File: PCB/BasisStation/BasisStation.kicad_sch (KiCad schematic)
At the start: 2 parts, among them U1 ESP32-S3-WROOM-1

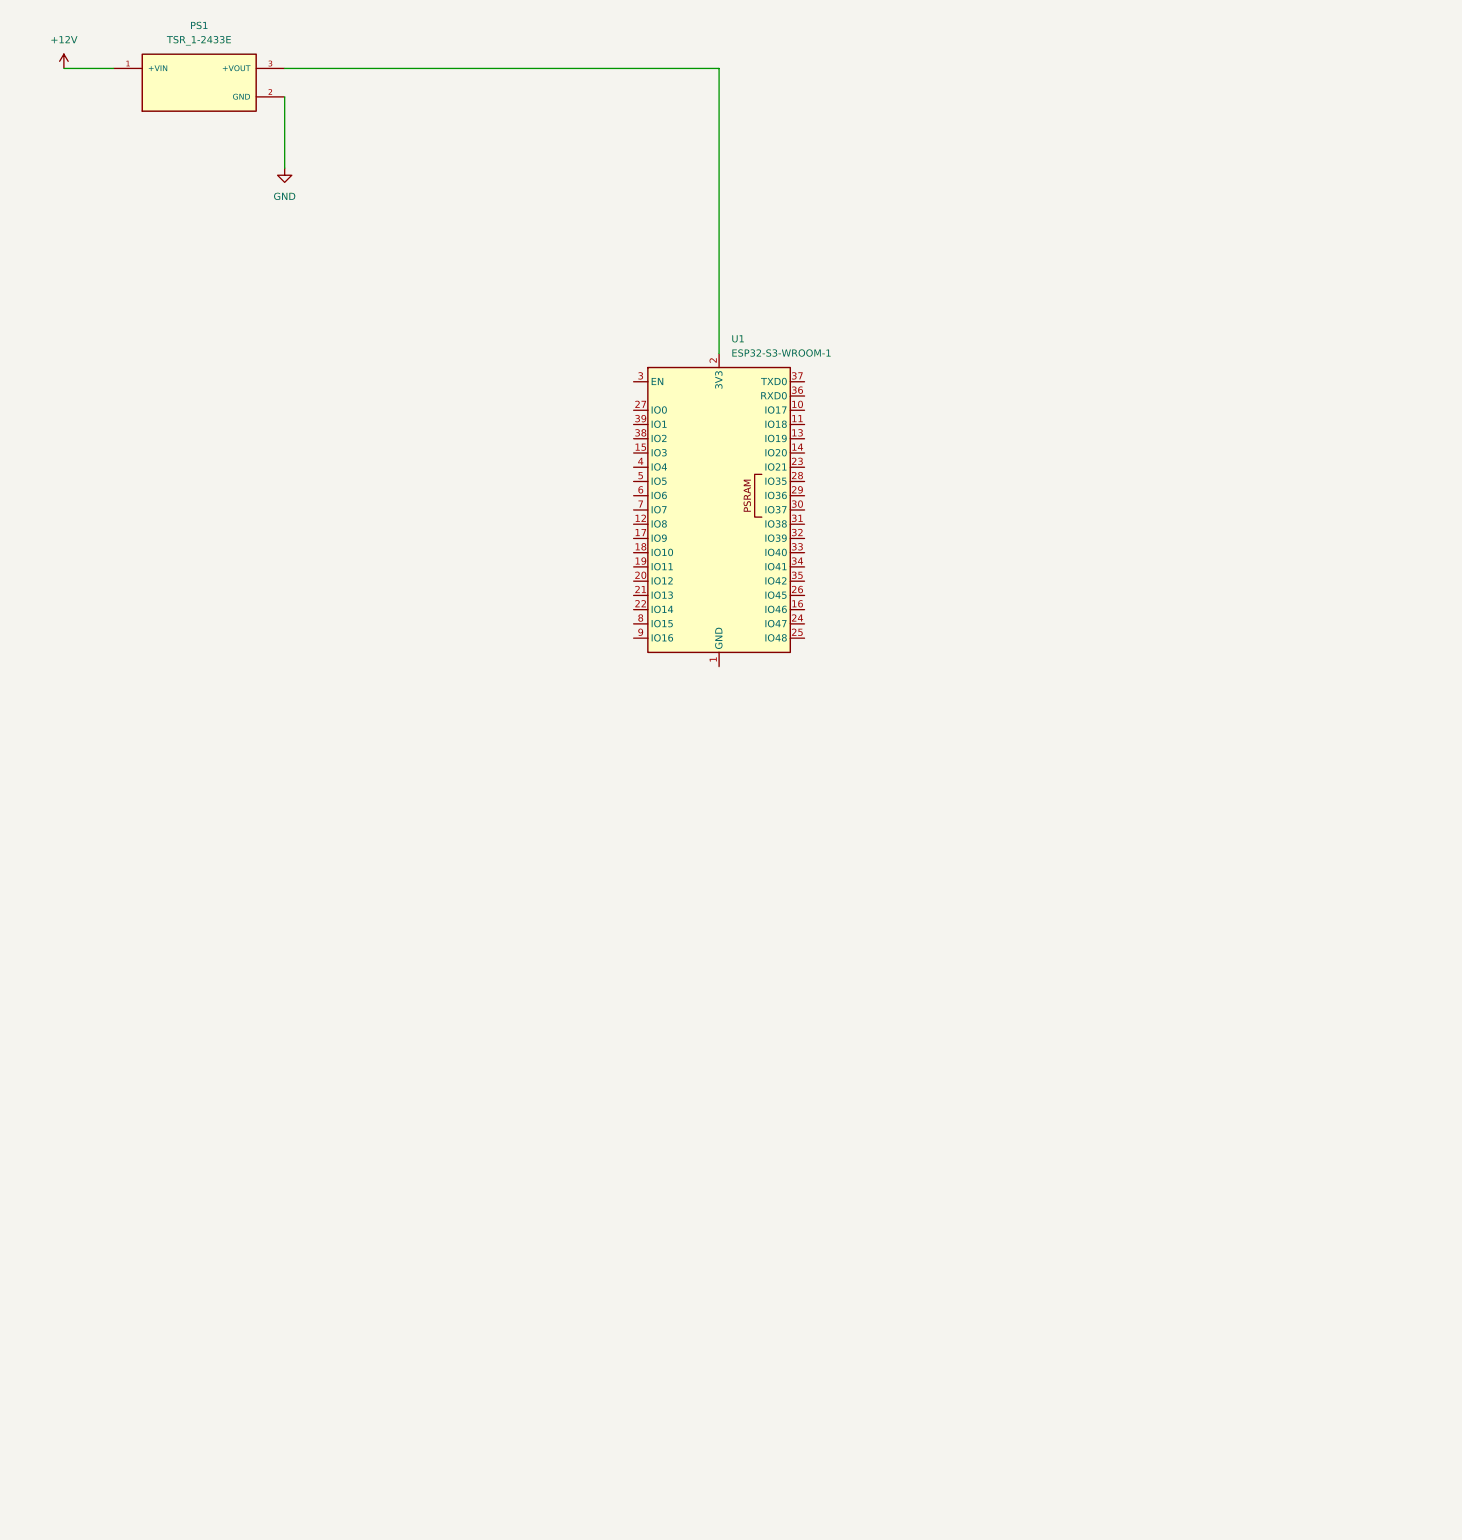
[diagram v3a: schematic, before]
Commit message: ESP32 Microcontroller geändert
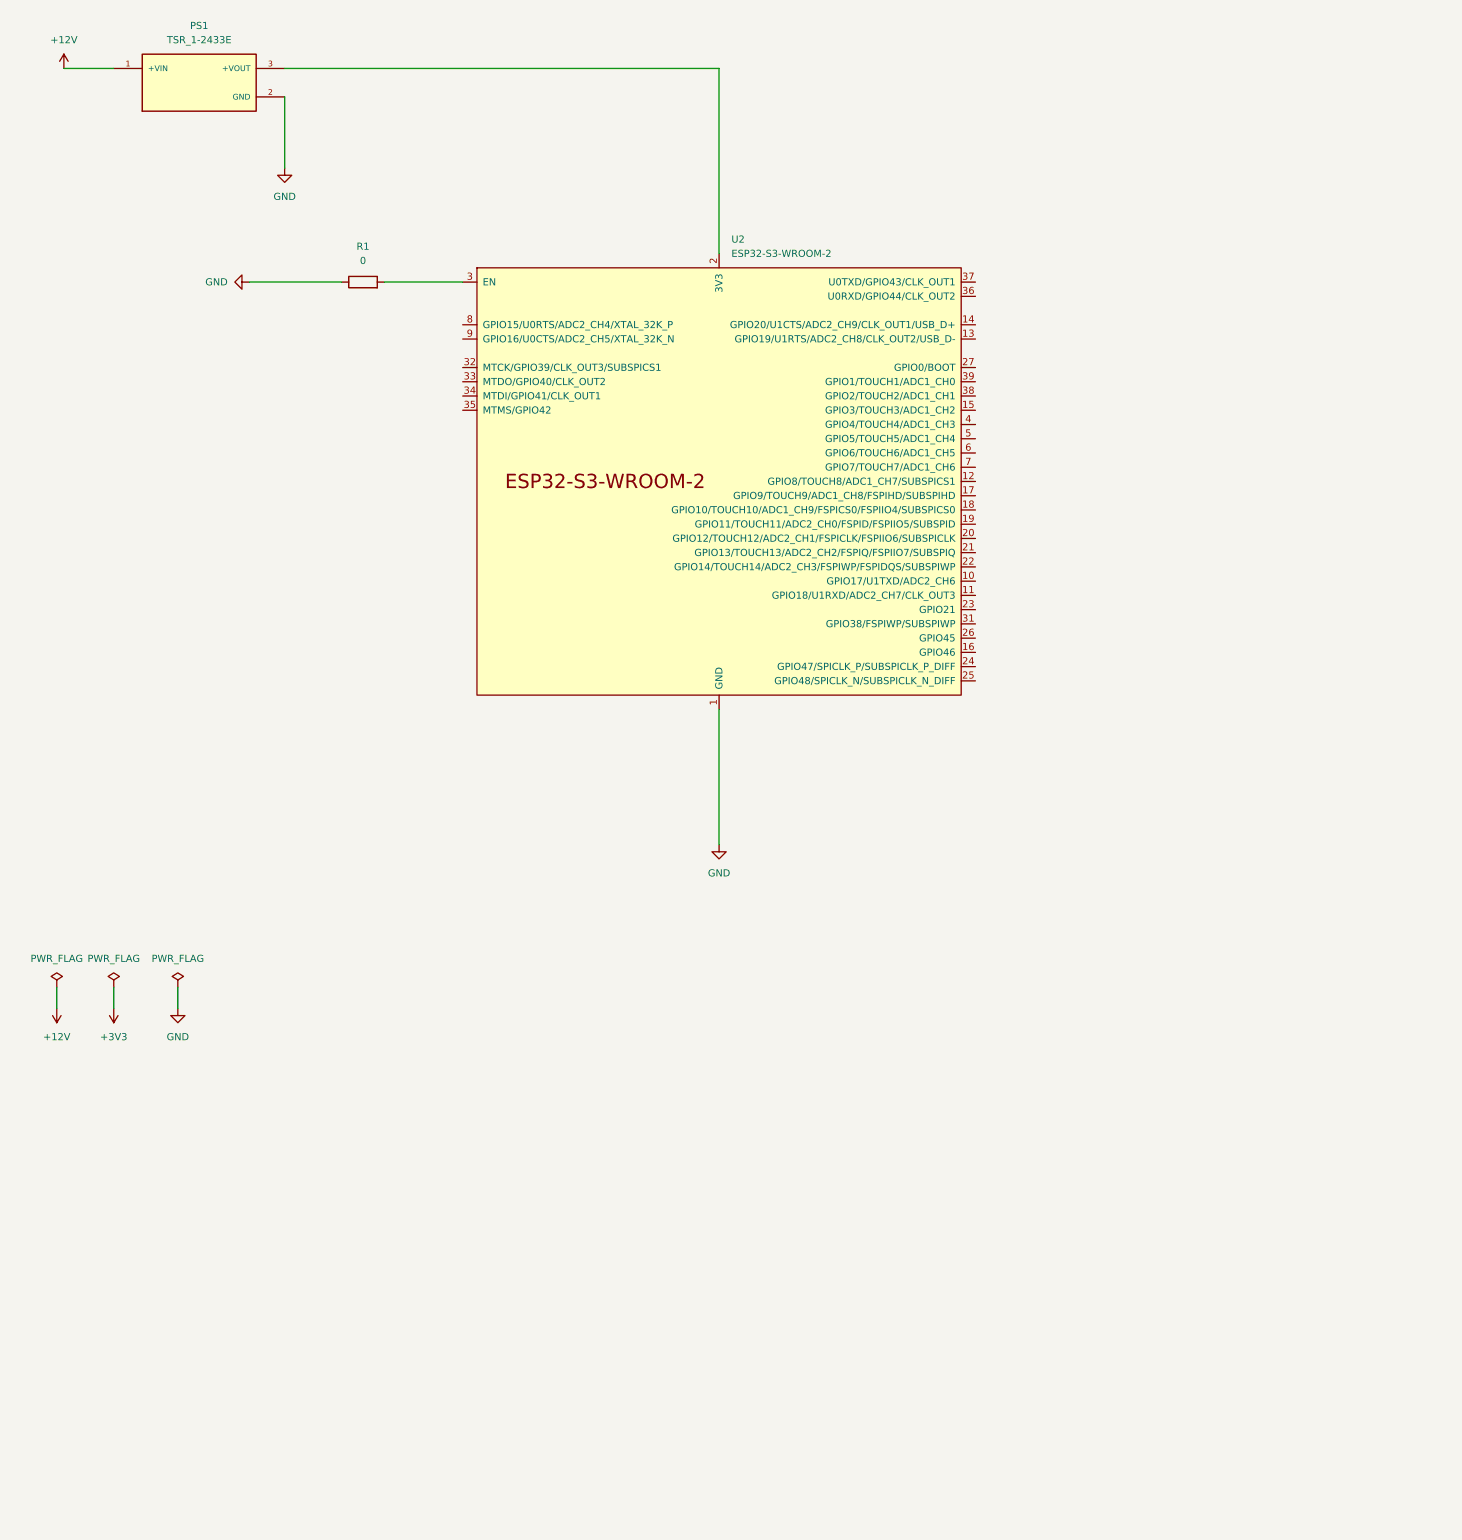
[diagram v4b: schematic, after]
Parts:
- removed U1: ESP32-S3-WROOM-1, RF_Module:ESP32-S3-WROOM-1, symbol RF_Module:ESP32-S3-WROOM-1
- added R1: 0, Resistor_THT:R_Axial_DIN0207_L6.3mm_D2.5mm_P10.16mm_Horizontal, symbol Device:R
- added U2: ESP32-S3-WROOM-2, PCM_Espressif:ESP32-S3-WROOM-2, symbol PCM_Espressif:ESP32-S3-WROOM-2
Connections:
- net GND: now also R1.1, U2.1 (GND), U2.40 (GND), U2.41 (GND)
- net at PS1.3 (+VOUT): now also U2.2 (3V3)
- new net: R1.2, U2.3 (EN)

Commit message: schaltplan überarbeitete
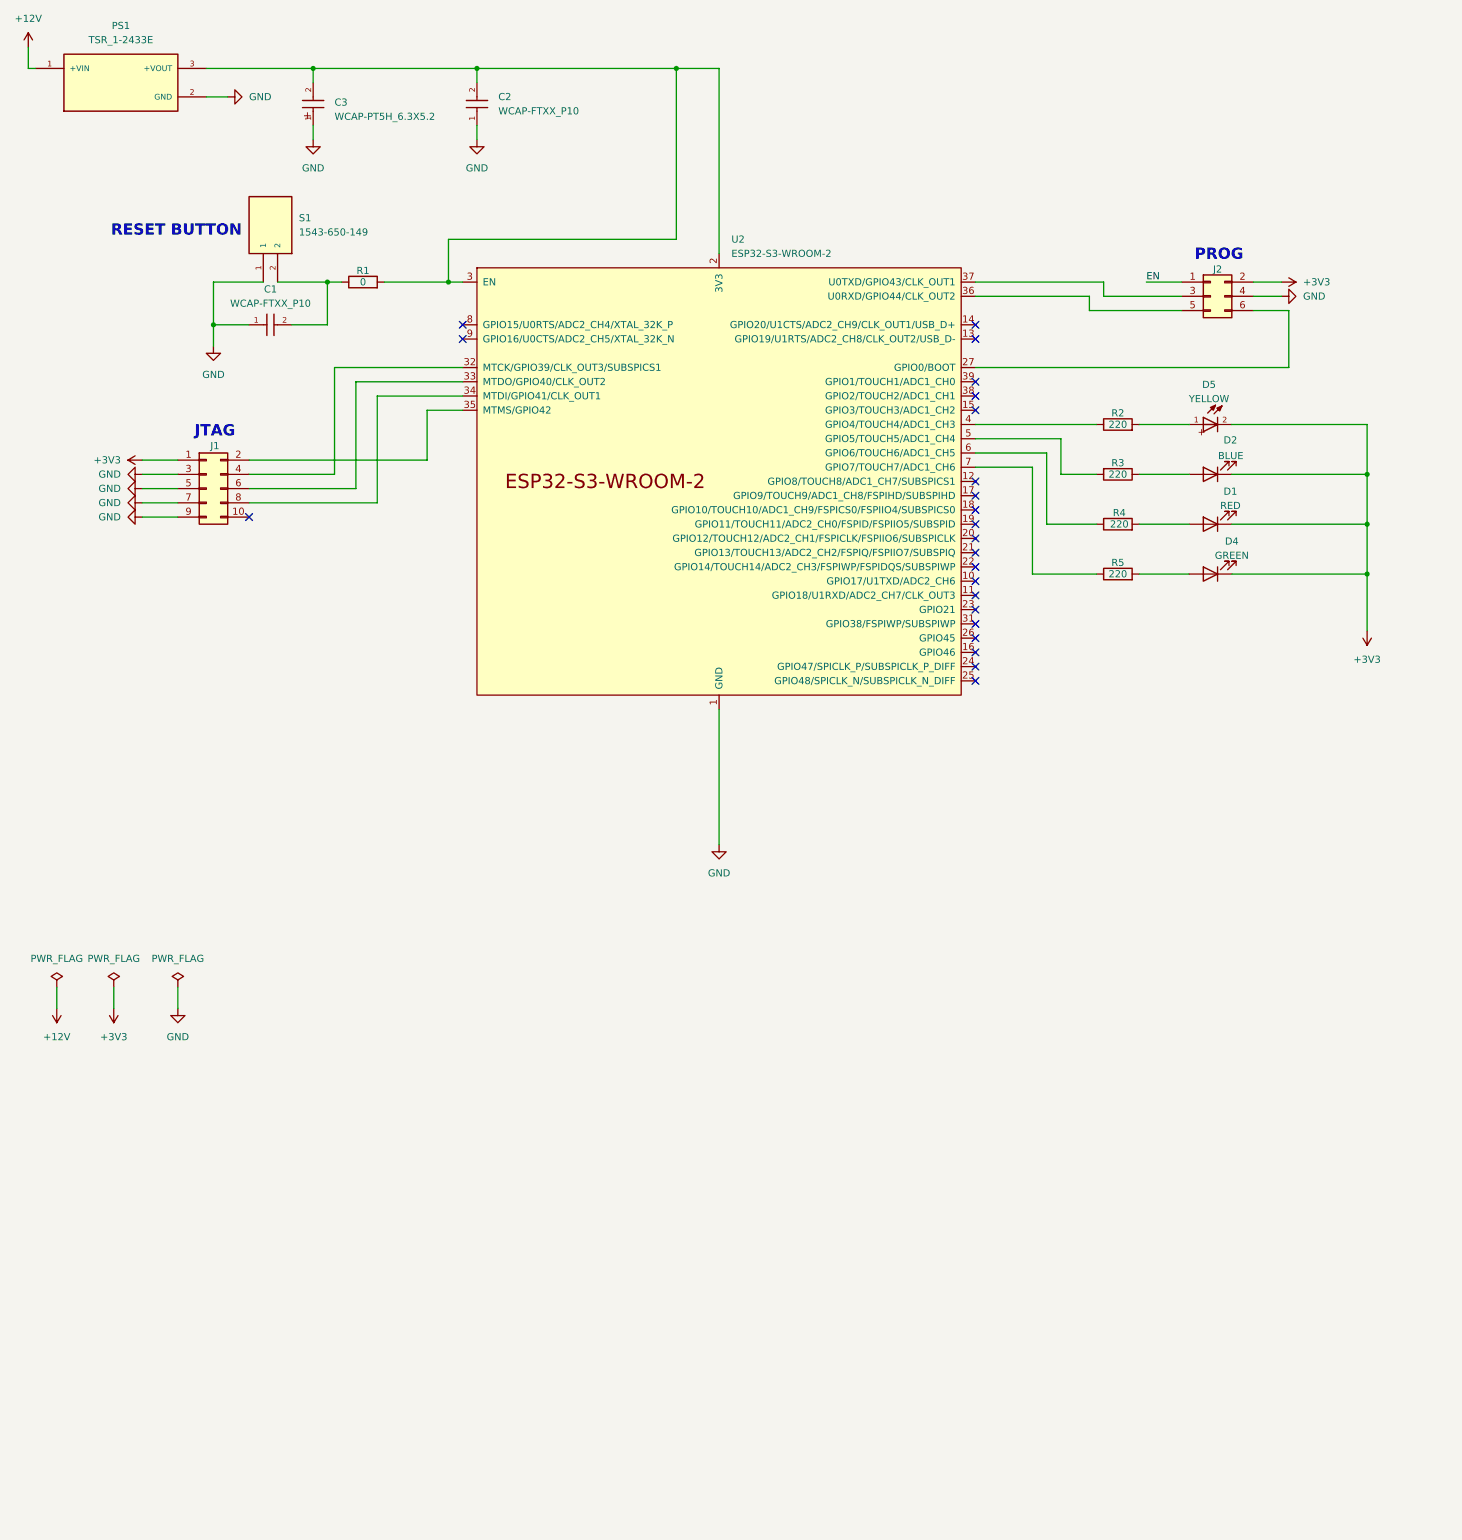
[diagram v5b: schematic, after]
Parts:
- added C1, C2: WCAP-FTXX_P10, Footprints:WCAP-FTXX_P10L13W7H13, symbol WCAP-FTXX_P10:WCAP-FTXX_P10
- added C3: WCAP-PT5H_6.3X5.2, Footprints:WCAP-PT5H_6.3X5.2_DXL_, symbol WCAP-PT5H_6.3X5.2:WCAP-PT5H_6.3X5.2
- added D1: RED, Footprints:WL-TMRW_3MM, symbol Device:LED
- added D2: BLUE, Footprints:WL-TMRW_3MM, symbol Device:LED
- added D4: GREEN, Footprints:WL-TMRC_3MM, symbol Device:LED
- added D5: YELLOW, Footprints:WL-TMRC_3MM, symbol WL-TMRC_3MM:WL-TMRC_3MM
- added J1: Conn_02x05_Odd_Even, Footprints:61201021621, symbol Connector_Generic:Conn_02x05_Odd_Even
- added J2: Conn_02x03_Odd_Even, symbol Connector_Generic:Conn_02x03_Odd_Even
- added R2, R3, R4, R5: 220, Resistor_THT:R_Axial_DIN0617_L17.0mm_D6.0mm_P20.32mm_Horizontal, symbol Device:R
- added S1: 1543-650-149, Footprints:1543650149, symbol 1543-650-149:1543-650-149
- U2: footprint PCM_Espressif:ESP32-S3-WROOM-2 -> Footprints:ESP32-S3-WROOM-2_NEW
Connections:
- net +3V3: now also D1.1 (K), D2.1 (K), D4.1 (K), D5.2, J1.1 (Pin_1), J2.2 (Pin_2)
- net GND: now also C1.1, C2.1, C3.1, J1.3 (Pin_3), J1.5 (Pin_5), J1.7 (Pin_7), J1.9 (Pin_9), J2.4 (Pin_4), S1.1; no longer R1.1
- net at PS1.3 (+VOUT), U2.2 (3V3): now also R1.2, U2.3 (EN), C2.2, C3.2
- net at U2.27 (GPIO0/BOOT): now also J2.6 (Pin_6)
- net at U2.32 (MTCK/GPIO39/CLK_OUT3/SUBSPICS1): now also J1.4 (Pin_4)
- net at U2.33 (MTDO/GPIO40/CLK_OUT2): now also J1.6 (Pin_6)
- net at U2.34 (MTDI/GPIO41/CLK_OUT1): now also J1.8 (Pin_8)
- net at U2.35 (MTMS/GPIO42): now also J1.2 (Pin_2)
- net at U2.36 (U0RXD/GPIO44/CLK_OUT2): now also J2.5 (Pin_5)
- net at U2.37 (U0TXD/GPIO43/CLK_OUT1): now also J2.3 (Pin_3)
- net at U2.4 (GPIO4/TOUCH4/ADC1_CH3): now also R2.1
- net at U2.5 (GPIO5/TOUCH5/ADC1_CH4): now also R3.2
- net at U2.6 (GPIO6/TOUCH6/ADC1_CH5): now also R4.1
- net at U2.7 (GPIO7/TOUCH7/ADC1_CH6): now also R5.1
- new net: D2.2 (A), R3.1
- new net: D1.2 (A), R4.2
- new net: D4.2 (A), R5.2
- new net: C1.2, R1.1, S1.2
- new net: D5.1, R2.2
- new net EN: J2.1 (Pin_1)
- no-connect marks 0 -> 23
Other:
- note added: "JTAG"
- note added: "PROG"
- note added: "RESET BUTTON"
- moved on the sheet: PS1

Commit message: 6Pin header male hinzugefügt und Leiterbahnen optimiert
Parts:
- J2: footprint (none) -> Footprints:61200621621
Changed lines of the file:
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@@
 			)
 		)
-		(property "Footprint" ""
+		(property "Footprint" "Footprints:61200621621"
 			(at 226.06 63.5 0)
 			(effects
